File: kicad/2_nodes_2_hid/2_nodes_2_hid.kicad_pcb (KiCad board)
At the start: 2 copper layers, 80 x 79.6 mm, 14 parts

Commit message: Update Kicad schematic, more compact design
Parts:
- moved Q_RST_0 30.2 mm to (92.0, 72.9)
- moved Q_RST_1 10.7 mm to (92.2, 62.8)
- moved HID_DEV_2 8.69 mm to (68.8, 117.8)
- moved Node1 8.69 mm to (72.3, 78.0)
- moved USB2_R1 8.69 mm to (62.4, 112.6)
- moved USB2_R2 8.69 mm to (82.0, 112.6)
- moved USB2_R3 8.69 mm to (71.1, 109.8)
- moved USB2_R4 8.69 mm to (73.9, 109.8)
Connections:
- Controller1 pad 13: /gnd_usb -> unconnected-(Controller1-GND-Pad13)
- Controller1 pad 38: /gnd -> Net-(Controller1-GND-Pad38)
- Controller1 pad 8: /gnd_usb -> GND1
- HID_DEV_1 pad 4: /gnd_usb -> GND1
- HID_DEV_2 pad 4: /gnd_usb -> GND1
- Node1 pad 3: /gnd -> Net-(Controller1-GND-Pad38)
- Node1 pad 38: Net-(Node1-GND-Pad38) -> GND
- Q_RST_0 pad 2: /gnd -> GND
- Q_RST_1 pad 2: Net-(Node1-GND-Pad38) -> GND
- USB1_R1 pad 1: /gnd_usb -> GND1
- USB1_R2 pad 2: /gnd_usb -> GND1
- USB2_R1 pad 1: /gnd_usb -> GND1
- USB2_R2 pad 2: /gnd_usb -> GND1
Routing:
- net GND1: track 0.00 -> 160.7 mm
- net /gnd_usb: track 160.7 -> 0.00 mm
- net Net-(Controller1-GPIO28_ADC2): track 11.2 -> 42.7 mm
- net /gnd: track 24.8 -> 0.00 mm
- net GND: track 0.00 -> 23.3 mm
- net Net-(Node1-GND-Pad38): track 12.6 -> 0.00 mm
- net Net-(Controller1-GND-Pad38): track 0.00 -> 12.5 mm
- net /vsys: track 151.8 -> 139.8 mm, vias 1 -> 0
- net /usb_2_dm: track 73.0 -> 61.0 mm
- net /usb_2_dp: track 77.4 -> 66.7 mm
- net /spi_clock: track 23.3 -> 14.6 mm, vias 2 -> 0
- net /spi_tx: track 21.2 -> 12.5 mm
- net /spi_sel: track 23.3 -> 14.6 mm
- net /spi_rx: track 21.2 -> 12.5 mm
- net /node_1_spi_ready: track 21.2 -> 12.5 mm
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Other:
- board size 80 x 79.6 mm -> 75 x 80 mm

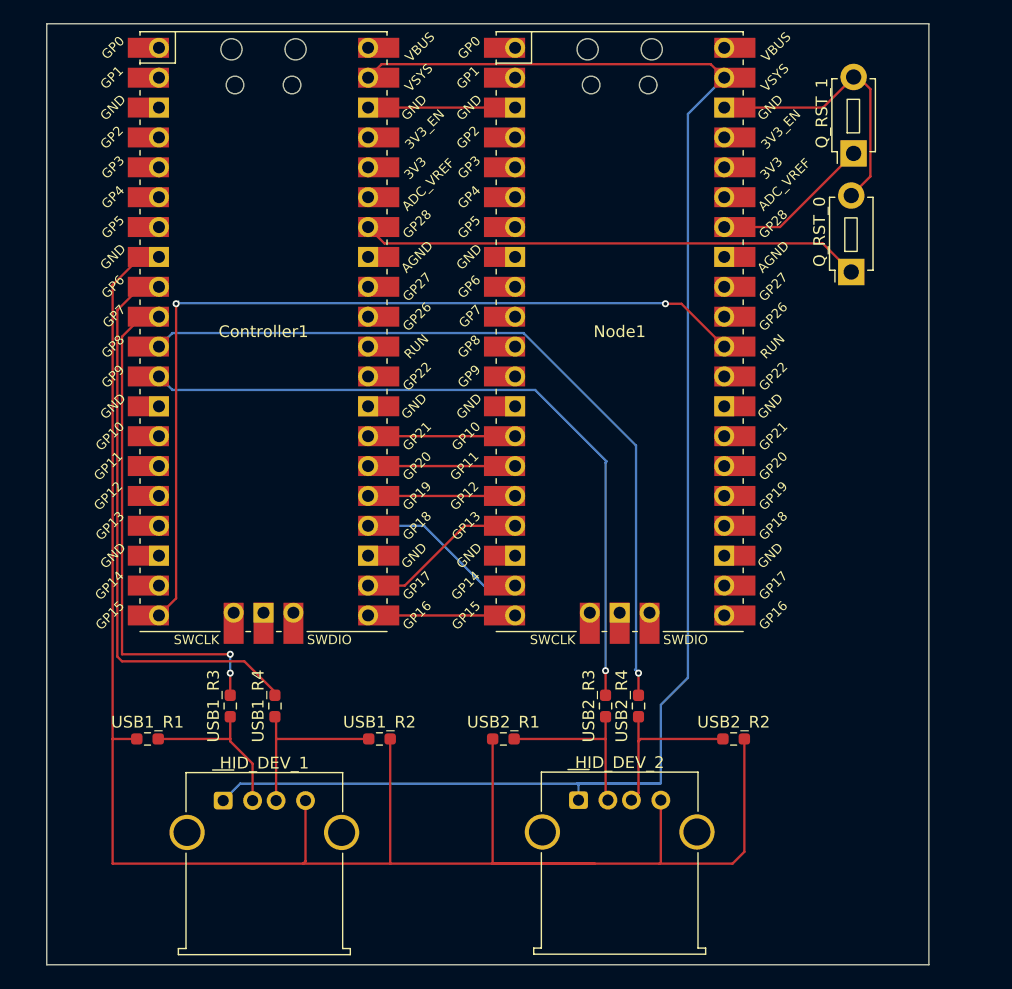
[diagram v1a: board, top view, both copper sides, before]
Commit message: Update PCB design, remove via on data tracks (inverted d+ and d-), add capacitor on usb ports
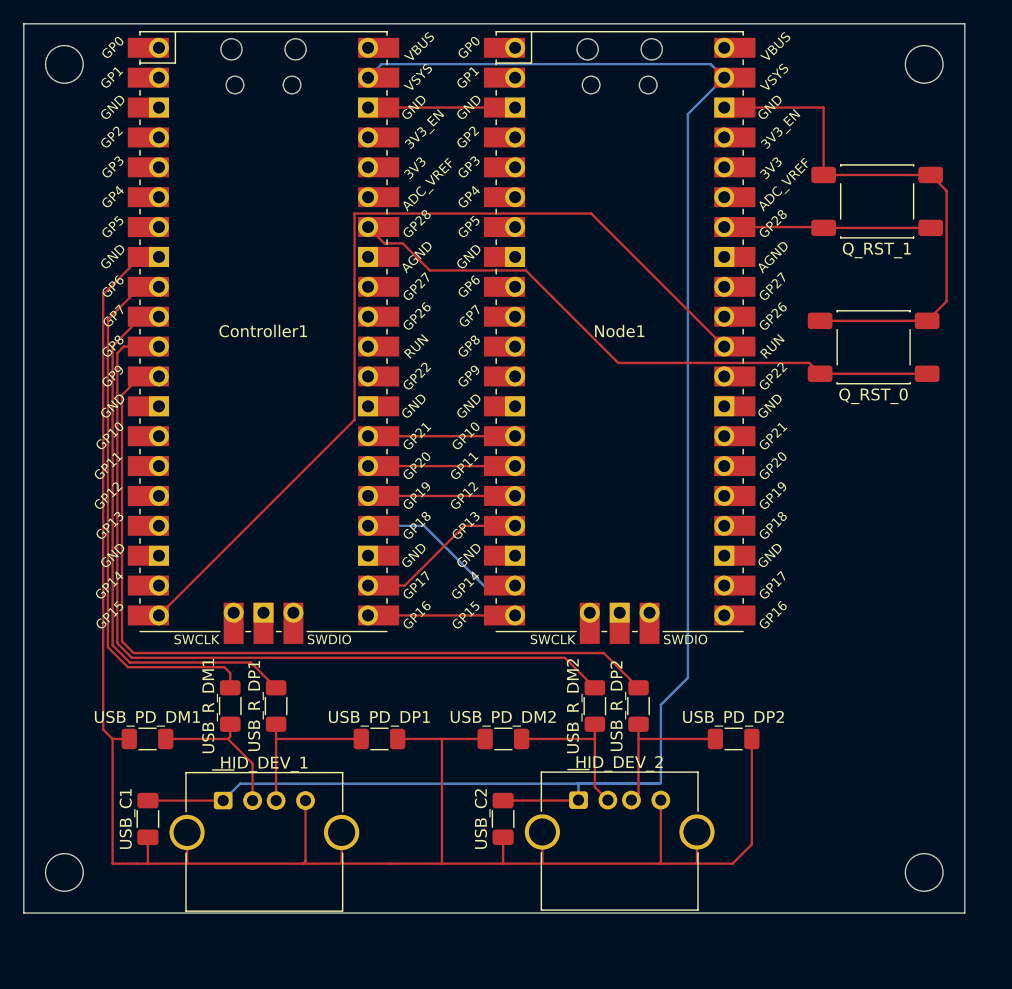
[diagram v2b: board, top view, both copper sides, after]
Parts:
- added REF**: MountingHole_3.2mm_M3, MountingHole:MountingHole_3.2mm_M3, F.Cu at (98.2, 124.0)
- added REF**: MountingHole_3.2mm_M3, MountingHole:MountingHole_3.2mm_M3, F.Cu at (98.2, 55.2)
- added REF**: MountingHole_3.2mm_M3, MountingHole:MountingHole_3.2mm_M3, F.Cu at (25.1, 124.0)
- added REF**: MountingHole_3.2mm_M3, MountingHole:MountingHole_3.2mm_M3, F.Cu at (25.1, 55.2)
- added USB_C1: 4.7 µF, Capacitor_SMD:C_1206_3216Metric_Pad1.33x1.80mm_HandSolder, F.Cu at (32.2, 119.4)
- added USB_C2: 4.7 µF, Capacitor_SMD:C_1206_3216Metric_Pad1.33x1.80mm_HandSolder, F.Cu at (62.4, 119.4)
- Q_RST_0, Q_RST_1: footprint Button_Switch_THT:SW_PUSH_1P1T_6x3.5mm_H4.3_APEM_MJTP1243 -> Button_Switch_SMD:SW_Push_1P1T_NO_E-Switch_TL3301NxxxxxG
- USB_PD_DM1: renamed from USB1_R1; footprint Resistor_SMD:R_0603_1608Metric_Pad0.98x0.95mm_HandSolder -> Resistor_SMD:R_1206_3216Metric_Pad1.30x1.75mm_HandSolder
- USB_PD_DM2: renamed from USB2_R1; footprint Resistor_SMD:R_0603_1608Metric_Pad0.98x0.95mm_HandSolder -> Resistor_SMD:R_1206_3216Metric_Pad1.30x1.75mm_HandSolder
- USB_PD_DP1: renamed from USB1_R2; footprint Resistor_SMD:R_0603_1608Metric_Pad0.98x0.95mm_HandSolder -> Resistor_SMD:R_1206_3216Metric_Pad1.30x1.75mm_HandSolder
- USB_PD_DP2: renamed from USB2_R2; footprint Resistor_SMD:R_0603_1608Metric_Pad0.98x0.95mm_HandSolder -> Resistor_SMD:R_1206_3216Metric_Pad1.30x1.75mm_HandSolder
- USB_R_DM1: renamed from USB1_R3; footprint Resistor_SMD:R_0603_1608Metric_Pad0.98x0.95mm_HandSolder -> Resistor_SMD:R_1206_3216Metric_Pad1.30x1.75mm_HandSolder
- USB_R_DM2: renamed from USB2_R3; footprint Resistor_SMD:R_0603_1608Metric_Pad0.98x0.95mm_HandSolder -> Resistor_SMD:R_1206_3216Metric_Pad1.30x1.75mm_HandSolder
- USB_R_DP1: renamed from USB1_R4; footprint Resistor_SMD:R_0603_1608Metric_Pad0.98x0.95mm_HandSolder -> Resistor_SMD:R_1206_3216Metric_Pad1.30x1.75mm_HandSolder
- USB_R_DP2: renamed from USB2_R4; footprint Resistor_SMD:R_0603_1608Metric_Pad0.98x0.95mm_HandSolder -> Resistor_SMD:R_1206_3216Metric_Pad1.30x1.75mm_HandSolder
- moved Q_RST_0 6.68 mm to (93.9, 79.3), turned to 180 degrees
- moved Q_RST_1 4.54 mm to (94.2, 66.9), turned to 180 degrees
- moved USB_R_DM2 0.91 mm to (70.2, 109.8)
- moved USB_R_DP1 0.10 mm to (43.1, 109.8)
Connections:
- Controller1 pad 10: /usb_1_dm -> /usb_1_dp
- Controller1 pad 11: /usb_2_dp -> /usb_2_dm
- Controller1 pad 12: /usb_2_dm -> /usb_2_dp
- Controller1 pad 9: /usb_1_dp -> /usb_1_dm
- HID_DEV_1 pad SH: unconnected-(HID_DEV_1-Shield-PadSH) -> GND1
- HID_DEV_2 pad SH: unconnected-(HID_DEV_2-Shield-PadSH) -> GND1
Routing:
- net GND: track 23.3 -> 46.0 mm
- net /vsys: track 139.8 -> 152.6 mm
- net Net-(Controller1-GPIO28_ADC2): track 42.7 -> 52.7 mm
- net /usb_2_dm: track 61.0 -> 70.6 mm, vias 1 -> 0
- net Net-(Node1-GPIO28_ADC2): track 13.6 -> 17.5 mm
- net GND1: track 160.7 -> 164.4 mm
- net /usb_2_dp: track 66.7 -> 70.3 mm, vias 1 -> 0
- net /usb_1_dp: track 48.8 -> 45.8 mm
- net /usb_1_dm: track 43.5 -> 45.9 mm, vias 2 -> 0
- net Net-(HID_DEV_2-D-): track 14.9 -> 13.1 mm
- net /node_reboot: track 75.5 -> 77.2 mm, vias 2 -> 0
- net Net-(HID_DEV_2-D+): track 14.6 -> 13.2 mm
- net Net-(HID_DEV_1-D+): track 15.0 -> 13.7 mm
- net Net-(HID_DEV_1-D-): track 14.0 -> 12.7 mm
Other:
- board size 75 x 80 mm -> 80 x 75.6 mm

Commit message: Rework PCB design, increase size of the VSYS track and GND to handle 100mA at 5V
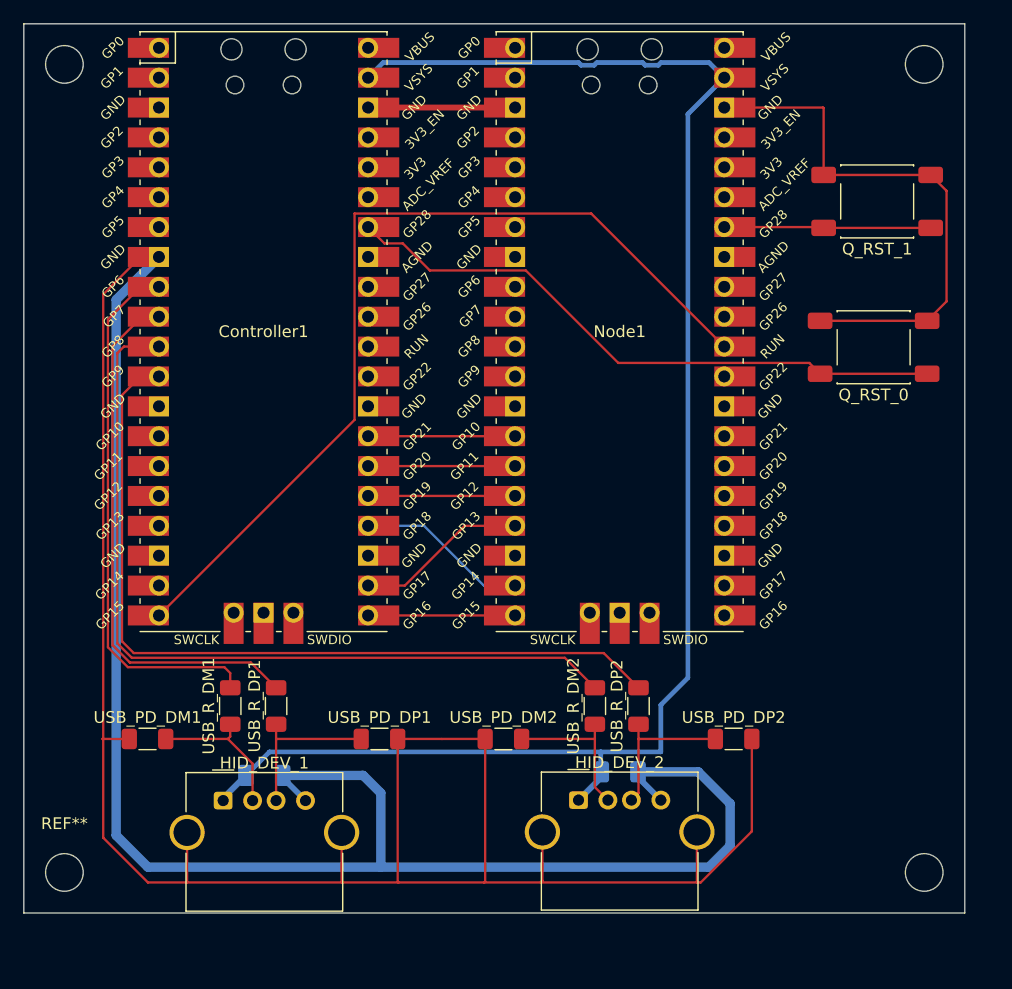
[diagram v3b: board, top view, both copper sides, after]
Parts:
- USB_C1, USB_C2: moved to B.Cu
- moved USB_C2 10.7 mm to (72.3, 115.4), turned to 180 degrees
- moved USB_C1 10.6 mm to (42.1, 115.7), turned to 180 degrees
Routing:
- net GND1: track 164.4 -> 310.0 mm
- net /vsys: track 152.6 -> 135.2 mm

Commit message: Rework PCB design, add ground plane, make sure d+ and d- track have same length and other various fix
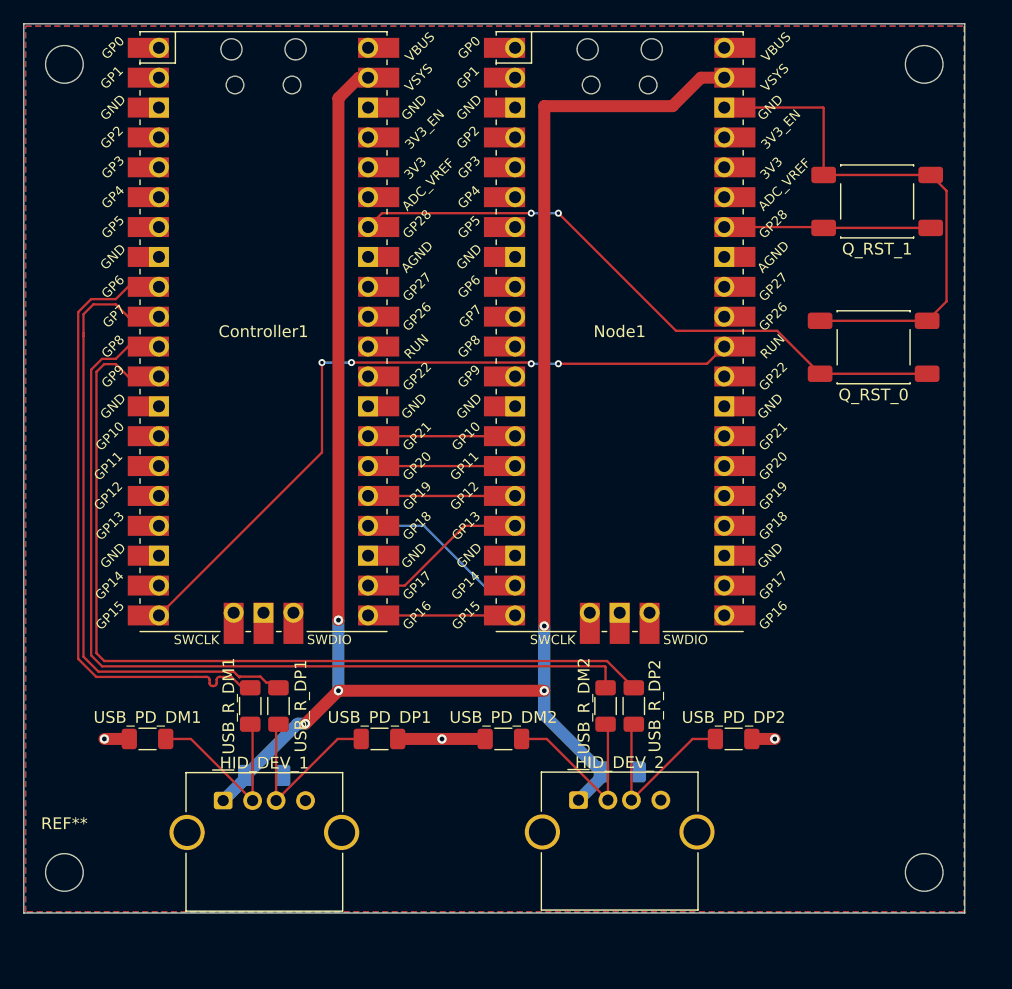
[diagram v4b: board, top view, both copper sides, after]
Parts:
- USB_C1, USB_C2: value 4.7 µF -> 10 µF
- moved USB_R_DM1 1.70 mm to (40.9, 109.8)
- moved USB_R_DM2 0.91 mm to (71.1, 109.8)
- moved USB_R_DP2 0.40 mm to (73.5, 109.8)
- moved USB_R_DP1 0.20 mm to (43.3, 109.8)
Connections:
- net /usb_1_dm renamed /usb_1_d-
- net /usb_1_dp renamed /usb_1_d+
- net /usb_2_dm renamed /usb_2_d-
- net /usb_2_dp renamed /usb_2_d+
- Controller1 pad 13: unconnected-(Controller1-GND-Pad13) -> GND
- Controller1 pad 18: unconnected-(Controller1-GND-Pad18) -> GND
- Controller1 pad 23: unconnected-(Controller1-GND-Pad23) -> GND
- Controller1 pad 28: unconnected-(Controller1-GND-Pad28) -> GND
- Controller1 pad 3: unconnected-(Controller1-GND-Pad3) -> GND
- Controller1 pad 33: unconnected-(Controller1-AGND-Pad33) -> GND
- Controller1 pad 38: Net-(Controller1-GND-Pad38) -> GND
- Controller1 pad 8: GND1 -> GND
- HID_DEV_1 pad 4: GND1 -> GND
- HID_DEV_1 pad SH: GND1 -> GND
- HID_DEV_2 pad 4: GND1 -> GND
- HID_DEV_2 pad SH: GND1 -> GND
- Node1 pad 13: unconnected-(Node1-GND-Pad13) -> GND
- Node1 pad 18: unconnected-(Node1-GND-Pad18) -> GND
- Node1 pad 23: unconnected-(Node1-GND-Pad23) -> GND
- Node1 pad 28: unconnected-(Node1-GND-Pad28) -> GND
- Node1 pad 3: Net-(Controller1-GND-Pad38) -> GND
- Node1 pad 33: unconnected-(Node1-AGND-Pad33) -> GND
- Node1 pad 8: unconnected-(Node1-GND-Pad8) -> GND
- USB_C1 pad 1: GND1 -> GND
- USB_C2 pad 1: GND1 -> GND
- USB_PD_DM1 pad 1: GND1 -> GND
- USB_PD_DM2 pad 1: GND1 -> GND
- USB_PD_DP1 pad 2: GND1 -> GND
- USB_PD_DP2 pad 2: GND1 -> GND
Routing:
- net GND1: track 310.0 -> 0.00 mm
- net /vsys: track 135.2 -> 163.7 mm, vias 0 -> 5
- net /node_reboot: track 77.2 -> 62.1 mm, vias 0 -> 4
- net Net-(Controller1-GND-Pad38): track 12.5 -> 0.00 mm
- net GND: track 46.0 -> 57.7 mm, vias 0 -> 3
- net /usb_1_d+: track 45.8 -> 54.0 mm
- net /usb_1_d-: track 45.9 -> 54.0 mm
- net /usb_2_d+: track 70.3 -> 76.8 mm
- net /usb_2_d-: track 70.6 -> 76.8 mm
- net Net-(HID_DEV_1-D-): track 12.7 -> 16.1 mm
- net Net-(HID_DEV_2-D-): track 13.1 -> 16.0 mm
- net Net-(HID_DEV_2-D+): track 13.2 -> 15.8 mm
- net Net-(HID_DEV_1-D+): track 13.7 -> 16.0 mm
- net Net-(Controller1-GPIO28_ADC2): track 52.7 -> 53.7 mm, vias 0 -> 2
- added copper zone on B.Cu, net GND
- added copper zone on F.Cu, net GND

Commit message: Fix error found by kicad DRC on the PCB
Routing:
- net /vsys: track 163.7 -> 162.5 mm
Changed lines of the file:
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@@
 	)
 	(segment
-		(start 67.1 80.7)
-		(end 79.74 80.7)
+		(start 64.79 80.7)
+		(end 64.69 80.6)
 		(width 0.2)
 		(layer "F.Cu")
@@
 	(segment
 		(start 64.69 80.6)
+		(end 49.51 80.6)
+		(width 0.2)
+		(layer "F.Cu")
+		(net "/node_reboot")
+	)
+	(segment
+		(start 66.89 80.7)
 		(end 64.79 80.7)
 		(width 0.2)
@@
 	)
 	(segment
-		(start 49.51 80.6)
-		(end 64.69 80.6)
+		(start 69.11 80.7)
+		(end 79.74 80.7)
 		(width 0.2)
 		(layer "F.Cu")
@@
 	)
 	(via
-		(at 67.1 80.7)
-		(size 0.6)
-		(drill 0.3)
-		(layers "F.Cu" "B.Cu")
-		(net "/node_reboot")
-	)
-	(via
-		(at 64.79 80.7)
+		(at 69.11 80.7)
+		(size 0.6)
+		(drill 0.3)
+		(layers "F.Cu" "B.Cu")
+		(net "/node_reboot")
+	)
+	(via
+		(at 66.89 80.7)
 		(size 0.6)
 		(drill 0.3)
@@
 	)
 	(segment
-		(start 64.79 80.7)
-		(end 67.1 80.7)
+		(start 66.89 80.7)
+		(end 69.11 80.7)
 		(width 0.2)
 		(layer "B.Cu")
@@
 	)
 	(segment
+		(start 66.89 67.9)
+		(end 52.1 67.9)
+		(width 0.2)
+		(layer "F.Cu")
+		(net "Net-(Controller1-GPIO28_ADC2)")
+	)
+	(segment
 		(start 98.45 81.55)
 		(end 89.35 81.55)
@@
 	)
 	(segment
-		(start 52.1 67.9)
-		(end 64.79 67.9)
+		(start 69.11 67.9)
+		(end 79.11 77.9)
+		(width 0.2)
+		(layer "F.Cu")
+		(net "Net-(Controller1-GPIO28_ADC2)")
+	)
+	(segment
+		(start 79.11 77.9)
+		(end 85.7 77.9)
 		(width 0.2)
 		(layer "F.Cu")
@@
 	)
 	(segment
-		(start 50.92 69.08)
-		(end 52.1 67.9)
-		(width 0.2)
-		(layer "F.Cu")
-		(net "Net-(Controller1-GPIO28_ADC2)")
-	)
-	(segment
-		(start 67.1 67.9)
-		(end 77.1 77.9)
-		(width 0.2)
-		(layer "F.Cu")
-		(net "Net-(Controller1-GPIO28_ADC2)")
-	)
-	(segment
-		(start 77.1 77.9)
-		(end 85.7 77.9)
-		(width 0.2)
-		(layer "F.Cu")
-		(net "Net-(Controller1-GPIO28_ADC2)")
-	)
-	(via
-		(at 67.1 67.9)
-		(size 0.6)
-		(drill 0.3)
-		(layers "F.Cu" "B.Cu")
-		(net "Net-(Controller1-GPIO28_ADC2)")
-	)
-	(via
-		(at 64.79 67.9)
-		(size 0.6)
-		(drill 0.3)
-		(layers "F.Cu" "B.Cu")
-		(net "Net-(Controller1-GPIO28_ADC2)")
-	)
-	(segment
-		(start 64.79 67.9)
-		(end 67.1 67.9)
+		(start 52.1 67.9)
+		(end 50.92 69.08)
+		(width 0.2)
+		(layer "F.Cu")
+		(net "Net-(Controller1-GPIO28_ADC2)")
+	)
+	(via
+		(at 69.11 67.9)
+		(size 0.6)
+		(drill 0.3)
+		(layers "F.Cu" "B.Cu")
+		(net "Net-(Controller1-GPIO28_ADC2)")
+	)
+	(via
+		(at 66.89 67.9)
+		(size 0.6)
+		(drill 0.3)
+		(layers "F.Cu" "B.Cu")
+		(net "Net-(Controller1-GPIO28_ADC2)")
+	)
+	(segment
+		(start 69.11 67.9)
+		(end 66.89 67.9)
 		(width 0.2)
 		(layer "B.Cu")
@@
 	)
 	(segment
-		(start 65.9 103)
-		(end 65.9 58.8)
-		(width 1.02)
-		(layer "F.Cu")
-		(net "/vsys")
-	)
-	(segment
-		(start 65.9 58.8)
-		(end 76.8 58.8)
-		(width 1.02)
-		(layer "F.Cu")
-		(net "/vsys")
-	)
-	(segment
 		(start 38.5975 117.8375)
 		(end 38.6 117.84)
@@
 	)
 	(segment
+		(start 76.8 58.8)
+		(end 79.22 56.38)
+		(width 1.02)
+		(layer "F.Cu")
+		(net "/vsys")
+	)
+	(segment
+		(start 68 58.8)
+		(end 76.8 58.8)
+		(width 1.02)
+		(layer "F.Cu")
+		(net "/vsys")
+	)
+	(segment
+		(start 65.9 103)
+		(end 68 100.9)
+		(width 1.02)
+		(layer "F.Cu")
+		(net "/vsys")
+	)
+	(segment
 		(start 65.9 108.5)
 		(end 48.4 108.5)
@@
 	)
 	(segment
-		(start 76.8 58.8)
-		(end 79.22 56.38)
+		(start 68 100.9)
+		(end 68 58.8)
 		(width 1.02)
 		(layer "F.Cu")
@@
 	)
 	(segment
+		(start 79.22 56.38)
+		(end 81.2 56.38)
+		(width 1.02)
+		(layer "F.Cu")
+		(net "/vsys")
+	)
+	(segment
 		(start 50.14 56.38)
 		(end 48.4 58.12)
@@
 		(width 1.02)
 		(layer "F.Cu")
-		(net "/vsys")
-	)
-	(segment
-		(start 79.22 56.38)
-		(end 81.2 56.38)
-		(width 1.02)
-		(layer "F.Cu")

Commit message: Add missing GND connection for debug pins
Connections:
- Controller1 pad 42: unconnected-(Controller1-GND-Pad42) -> GND
- Node1 pad 42: unconnected-(Node1-GND-Pad42) -> GND
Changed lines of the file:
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@@
 			(layers "*.Cu" "*.Mask")
 			(remove_unused_layers no)
-			(net "unconnected-(Controller1-GND-Pad42)")
+			(net "GND")
 			(pinfunction "GND_42")
 			(pintype "power_in")
@@
 			)
 			(layers "F.Cu" "F.Mask")
-			(net "unconnected-(Controller1-GND-Pad42)")
+			(net "GND")
 			(pinfunction "GND_42")
 			(pintype "power_in")
@@
 			(layers "*.Cu" "*.Mask")
 			(remove_unused_layers no)
-			(net "unconnected-(Node1-GND-Pad42)")
+			(net "GND")
 			(pinfunction "GND_42")
 			(pintype "power_in")
@@
 			)
 			(layers "F.Cu" "F.Mask")
-			(net "unconnected-(Node1-GND-Pad42)")
+			(net "GND")
 			(pinfunction "GND_42")
 			(pintype "power_in")
